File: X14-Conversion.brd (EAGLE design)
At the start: 160 x 100 mm, 23 parts, among them P1 282837-2, P2 282837-2, P3 282837-2, U2 LM2678SD-ADJ/NOPB

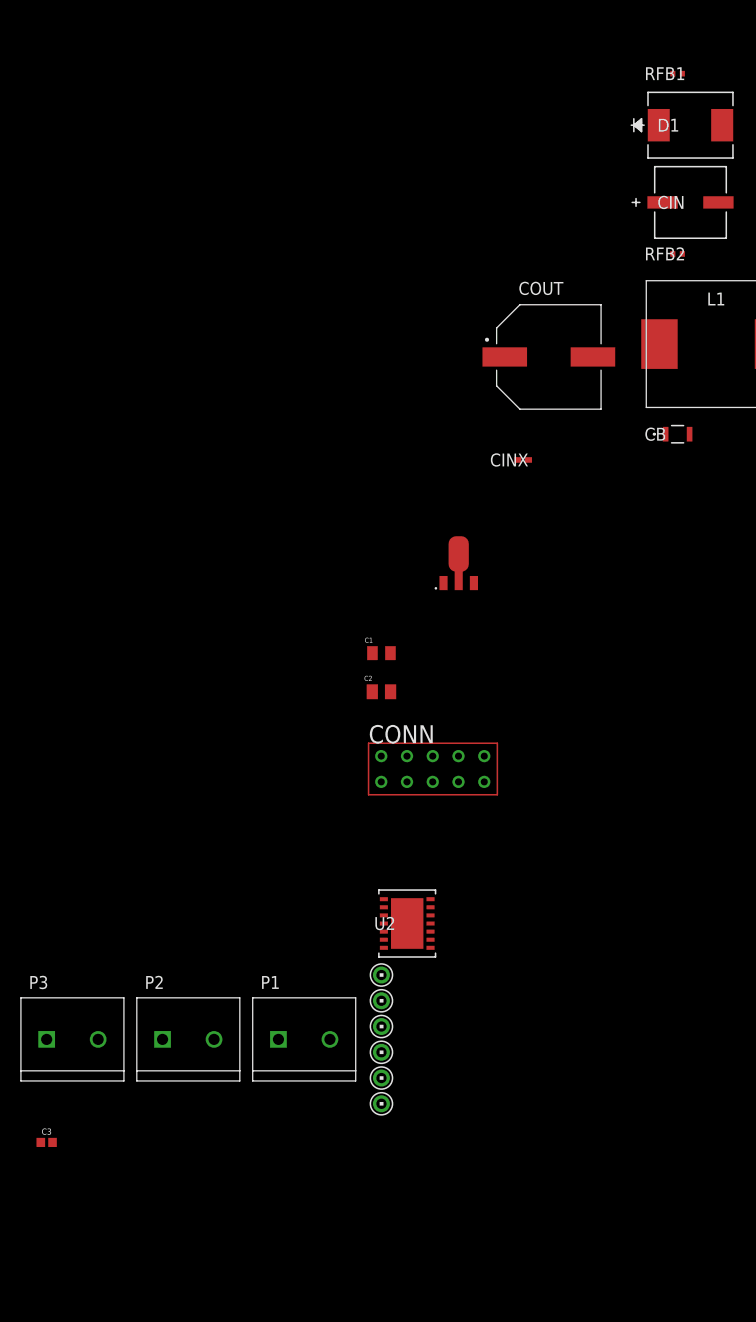
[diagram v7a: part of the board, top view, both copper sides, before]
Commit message: Fix capacitors and resistors to Sparkfun components
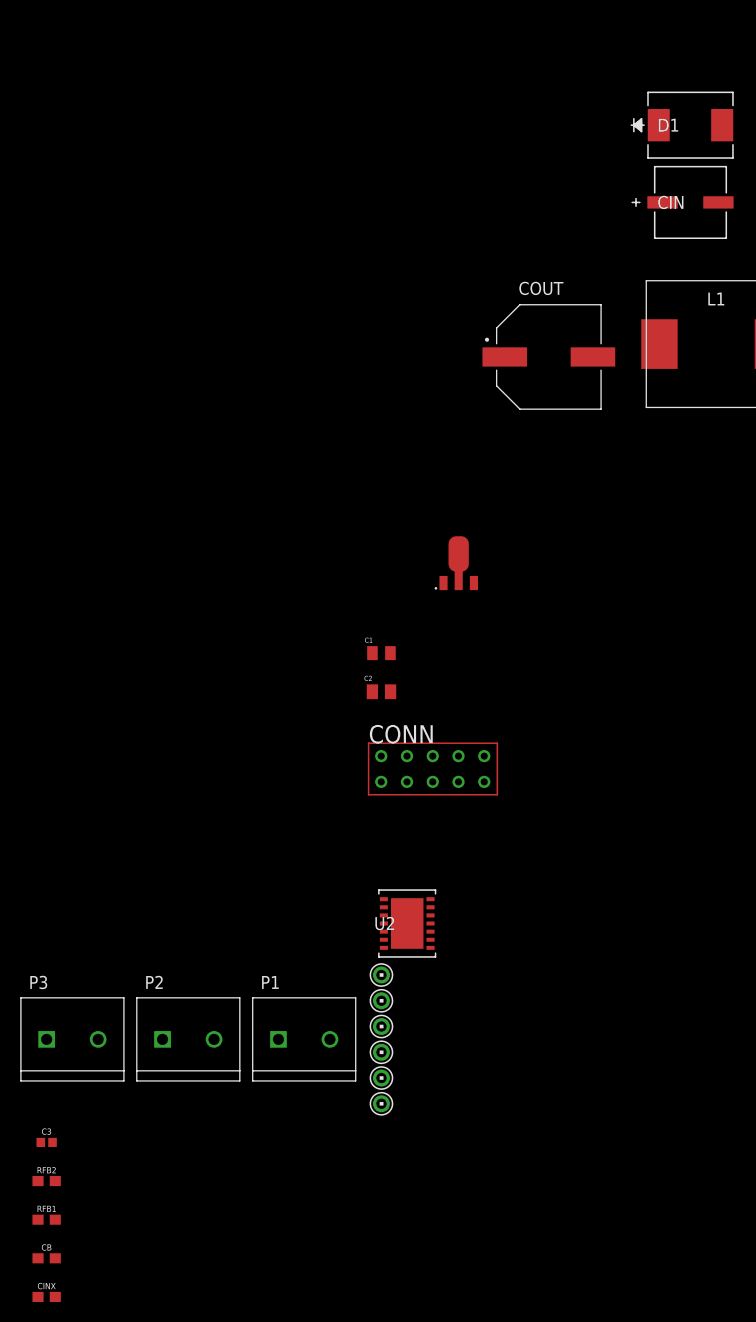
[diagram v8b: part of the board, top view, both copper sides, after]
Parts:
- CB: device CGA4C2C0G1H103J060AA:CAP_2012_TDK -> SparkFun-Capacitors:0603
- CINX: value 100nF 1mΩ -> 0.1uF 1mΩ; device GRM155R71C104KA88D:CAP_GRM_155_MUR -> SparkFun-Capacitors:0603
- RFB1: device CRCW04021K00FKED:RES_CRCW_0402 -> SparkFun-Resistors:0603
- RFB2: device CRCW04023K32FKED:RES_CRCW_0402 -> SparkFun-Resistors:0603
- moved RFB1 129.0 mm to (-92.7, -33.0)
- moved RFB2 110.6 mm to (-92.7, -29.2)
- moved CB 102.4 mm to (-92.7, -36.8)
- moved CINX 95.0 mm to (-92.7, -40.6)
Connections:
- net 5.2V: now also RFB2.2; no longer RFB2.1
- net GND: now also RFB1.2; no longer RFB1.1
- net N$5: now also RFB1.1, RFB2.1; no longer RFB1.2, RFB2.2
